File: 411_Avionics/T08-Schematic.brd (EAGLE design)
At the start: 65.8 x 25.4 mm, 68 parts, among them IC1 BQ24022, J1 USB-MICROB, J3 JST-PH-2-SMT-RA, U1 LP5907, U2 M25P10-AVMN6TP_TR, U3 LSM9DS0, U5 LTC1998, U6 ATMEGA32U4-AU, X1 8MHz

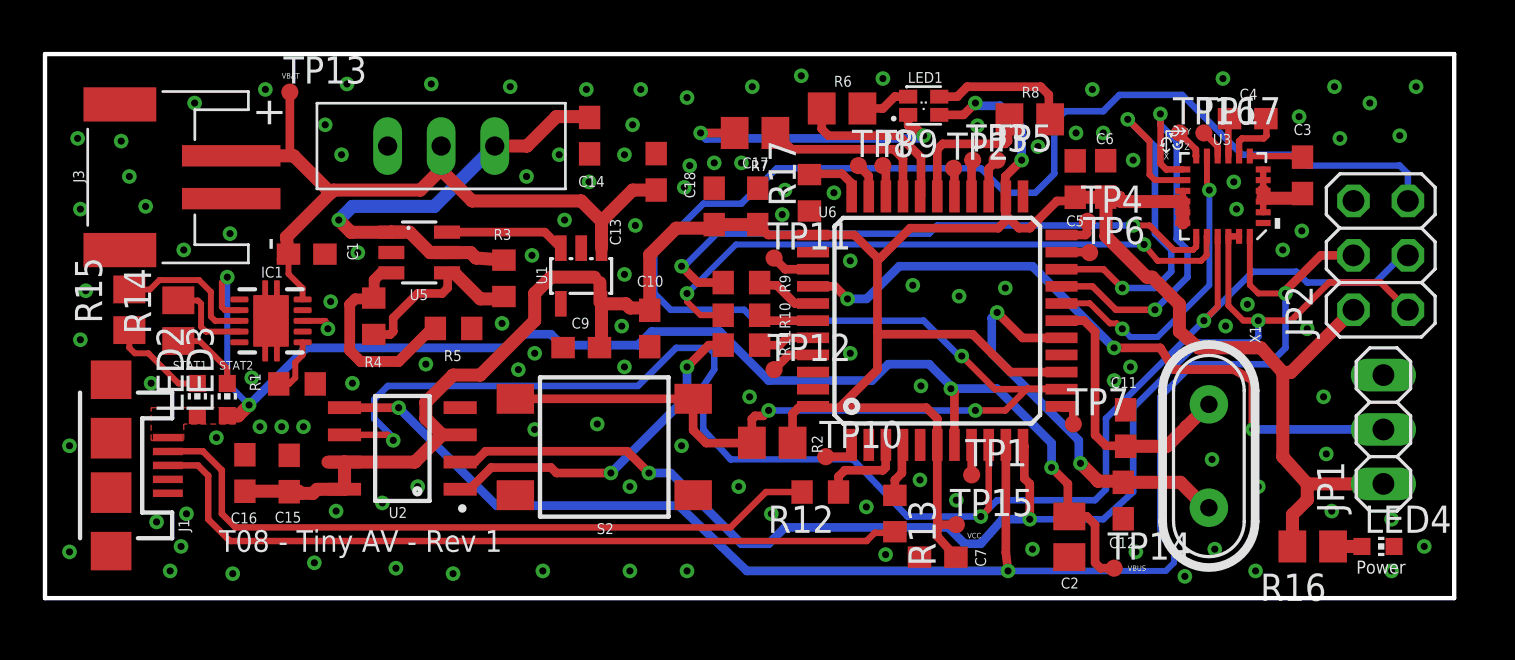
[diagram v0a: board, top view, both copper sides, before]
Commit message: Some silk screen touches to  BRD file.
Ready to ship off.
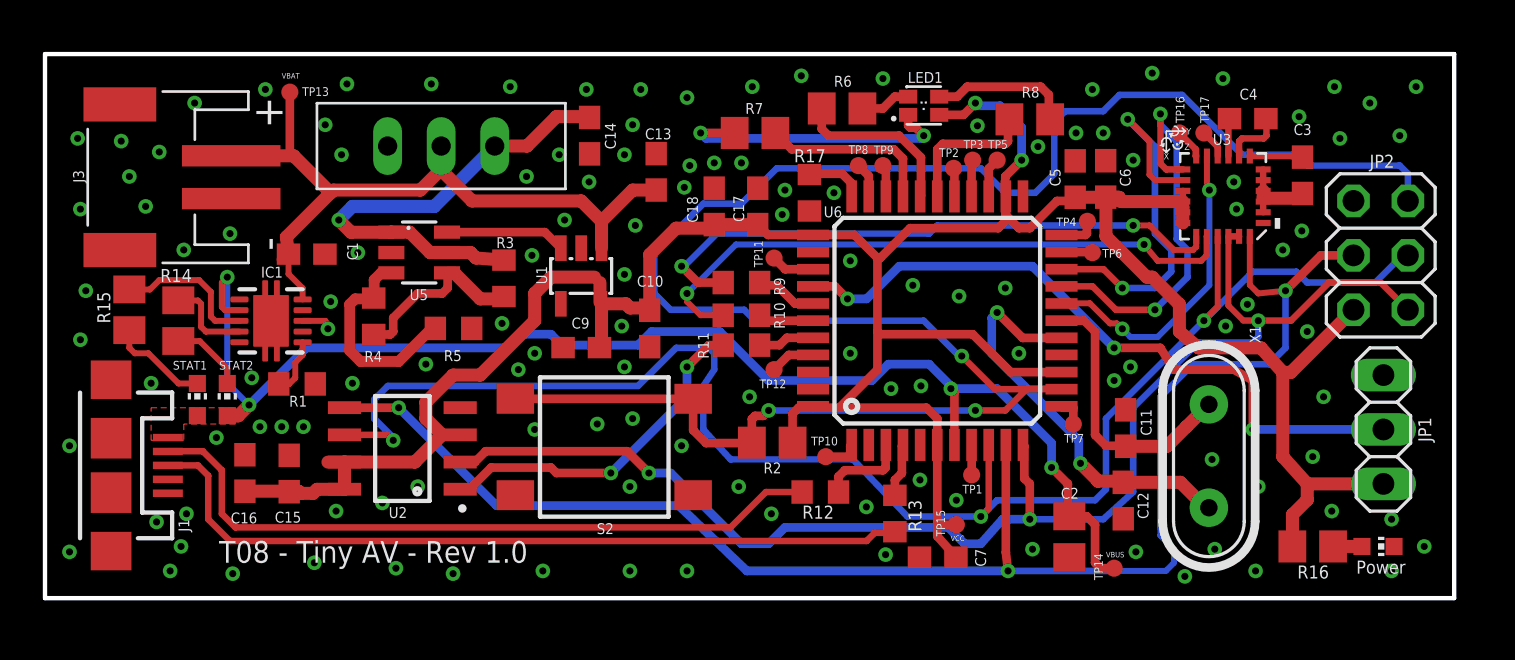
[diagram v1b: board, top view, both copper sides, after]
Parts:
- moved TP6 0.13 mm to (48.9, 16.1)
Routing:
- net GND: vias 122 -> 127
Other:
- board text added: "T08 - Tiny AV - Rev 1.0"
- board text removed: "T08 - Tiny AV - Rev 1"
